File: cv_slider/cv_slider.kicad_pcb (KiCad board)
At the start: 2 copper layers, 47 x 8.2 mm, 12 parts, among them J1 I/O connector, U1 HT7550-1, U2 TLV6001UIDBVR

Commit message: Added 1k output resistor
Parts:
- added R2: 10K, Resistor_SMD:R_0402_1005Metric, F.Cu at (155.4, 81.6)
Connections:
- U2 pad 3: OUT -> Net-(U2-Pad3)
- U2 pad 4: OUT -> Net-(U2-Pad3)
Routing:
- net Net-(U2-Pad3): track 0.00 -> 20.1 mm, vias 0 -> 2
- net OUT: track 21.2 -> 3.26 mm, vias 2 -> 0
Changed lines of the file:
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@@
   (net 6 "OUT")
   (net 7 "Net-(JP1-Pad2)")
+  (net 8 "Net-(U2-Pad3)")
+  (footprint "Resistor_SMD:R_0402_1005Metric" (layer "F.Cu")
+    (at 155.4 81.6 -90)
+    (descr "Resistor SMD 0402 (1005 Metric), square (rectangular) end terminal, IPC_7351 nominal, (Body size source: IPC-SM-782 page 72, https://www.pcb-3d.com/wordpress/wp-content/uploads/ipc-sm-782a_amendment_1_and_2.pdf), generated with kicad-footprint-generator")
+    (tags "resistor")
+    (property "LCSC" "C11702")
+    (property "Sheetfile" "File: cv_slider.kicad_sch")
+    (property "Sheetname" "")
+    (attr smd)
+    (fp_text reference "R2" (at 0 -1.17 90) (layer "F.SilkS") hide
+      (effects (font (size 1 1) (thickness 0.15)))
+    )
+    (fp_text value "10K" (at 0 1.17 90) (layer "F.Fab")
+      (effects (font (size 1 1) (thickness 0.15)))
+    )
+    (fp_text user "${REFERENCE}" (at 0 0 90) (layer "F.Fab")
+      (effects (font (size 0.26 0.26) (thickness 0.04)))
+    )
+    (fp_line (start -0.153641 -0.38) (end 0.153641 -0.38) (layer "F.SilkS") (width 0.12))
+    (fp_line (start -0.153641 0.38) (end 0.153641 0.38) (layer "F.SilkS") (width 0.12))
+    (fp_line (start -0.93 0.47) (end -0.93 -0.47) (layer "F.CrtYd") (width 0.05))
+    (fp_line (start -0.93 -0.47) (end 0.93 -0.47) (layer "F.CrtYd") (width 0.05))
+    (fp_line (start 0.93 -0.47) (end 0.93 0.47) (layer "F.CrtYd") (width 0.05))
+    (fp_line (start 0.93 0.47) (end -0.93 0.47) (layer "F.CrtYd") (width 0.05))
+    (fp_line (start -0.525 0.27) (end -0.525 -0.27) (layer "F.Fab") (width 0.1))
+    (fp_line (start -0.525 -0.27) (end 0.525 -0.27) (layer "F.Fab") (width 0.1))
+    (fp_line (start 0.525 0.27) (end -0.525 0.27) (layer "F.Fab") (width 0.1))
+    (fp_line (start 0.525 -0.27) (end 0.525 0.27) (layer "F.Fab") (width 0.1))
+    (pad "1" smd roundrect (at -0.51 0 270) (size 0.54 0.64) (layers "F.Cu" "F.Paste" "F.Mask") (roundrect_rratio 0.25)
+      (net 8 "Net-(U2-Pad3)") (pintype "passive"))
+    (pad "2" smd roundrect (at 0.51 0 270) (size 0.54 0.64) (layers "F.Cu" "F.Paste" "F.Mask") (roundrect_rratio 0.25)
+      (net 6 "OUT") (pintype "passive"))
+    (model "${KICAD6_3DMODEL_DIR}/Resistor_SMD.3dshapes/R_0402_1005Metric.wrl"
+      (offset (xyz 0 0 0))
+      (scale (xyz 1 1 1))
+      (rotate (xyz 0 0 0))
+    )
+  )
   (footprint "cycfi_library:pin_header_1x3p_2.54mm_smd_horizontal" (layer "F.Cu")
     (at 152.8 83.7 180)
@@
     (descr "SOT, 5 Pin (https://www.jedec.org/sites/default/files/docs/Mo-178c.PDF variant AA), generated with kicad-footprint-generator ipc_gullwing_generator.py")
     (tags "SOT TO_SOT_SMD")
+    (property "LCSC" "C544299")
     (property "Sheetfile" "File: cv_slider.kicad_sch")
     (property "Sheetname" "")
@@
       (net 2 "GND") (pinfunction "V-") (pintype "power_in"))
     (pad "3" smd roundrect (at -1.1375 0.95 270) (size 1.325 0.6) (layers "F.Cu" "F.Paste" "F.Mask") (roundrect_rratio 0.25)
-      (net 6 "OUT") (pinfunction "-") (pintype "input"))
+      (net 8 "Net-(U2-Pad3)") (pinfunction "-") (pintype "input"))
     (pad "4" smd roundrect (at 1.1375 0.95 270) (size 1.325 0.6) (layers "F.Cu" "F.Paste" "F.Mask") (roundrect_rratio 0.25)
-      (net 6 "OUT") (pintype "output"))
+      (net 8 "Net-(U2-Pad3)") (pintype "output"))
     (pad "5" smd roundrect (at 1.1375 -0.95 270) (size 1.325 0.6) (layers "F.Cu" "F.Paste" "F.Mask") (roundrect_rratio 0.25)
       (net 3 "5v") (pinfunction "V+") (pintype "power_in"))
@@
     )
   )
-  (footprint "cycfi_library:cycfi-logo-9mm" locked (layer "F.Cu")
+  (footprint "cycfi_library:cycfi-logo-9mm" (layer "F.Cu")
     (at 141.5 83)
-    (attr through_hole)
+    (attr through_hole board_only)
     (fp_text reference "G***" (at 0 0) (layer "F.SilkS") hide
       (effects (font (size 1.524 1.524) (thickness 0.3)))
@@
   (segment (start 152.8 78.62) (end 155.63 78.62) (width 0.4084) (layer "F.Cu") (net 5))
   (segment (start 155.63 78.62) (end 155.65 78.6) (width 0.4084) (layer "F.Cu") (net 5))
-  (segment (start 169.5125 82.3375) (end 168.85 83) (width 0.4084) (layer "F.Cu") (net 6))
-  (segment (start 155.25 82.35) (end 154.15 82.35) (width 0.4084) (layer "F.Cu") (net 6))
-  (segment (start 154.15 82.35) (end 152.8 83.7) (width 0.4084) (layer "F.Cu") (net 6))
-  (segment (start 170.05 82.3375) (end 170.05 80.0625) (width 0.4084) (layer "F.Cu") (net 6))
-  (segment (start 170.05 82.3375) (end 169.5125 82.3375) (width 0.4084) (layer "F.Cu") (net 6))
-  (via (at 168.85 83) (size 0.6) (drill 0.4) (layers "F.Cu" "B.Cu") (net 6))
-  (via (at 155.25 82.35) (size 0.6) (drill 0.4) (layers "F.Cu" "B.Cu") (net 6))
-  (segment (start 155.9542 81.6458) (end 155.25 82.35) (width 0.4084) (layer "B.Cu") (net 6))
-  (segment (start 167.4958 81.6458) (end 155.9542 81.6458) (width 0.4084) (layer "B.Cu") (net 6))
-  (segment (start 168.85 83) (end 167.4958 81.6458) (width 0.4084) (layer "B.Cu") (net 6))
+  (segment (start 154.39 82.11) (end 155.4 82.11) (width 0.4084) (layer "F.Cu") (net 6))
+  (segment (start 152.8 83.7) (end 154.39 82.11) (width 0.4084) (layer "F.Cu") (net 6))
   (segment (start 168 81.56) (end 168 83.7) (width 0.4084) (layer "F.Cu") (net 7))
   (segment (start 167.1 84.6) (end 164.575 84.6) (width 0.4084) (layer "F.Cu") (net 7))
   (segment (start 168 83.7) (end 167.1 84.6) (width 0.4084) (layer "F.Cu") (net 7))
   (segment (start 164.575 84.6) (end 163.875 83.9) (width 0.4084) (layer "F.Cu") (net 7))
+  (segment (start 155.3 80.1) (end 155.3 80.99) (width 0.4084) (layer "F.Cu") (net 8))
+  (segment (start 155.3 80.99) (end 155.4 81.09) (width 0.4084) (layer "F.Cu") (net 8))
+  (segment (start 169.5125 82.3375) (end 168.85 83) (width 0.4084) (layer "F.Cu") (net 8))
+  (segment (start 170.05 82.3375) (end 170.05 80.0625) (width 0.4084) (layer "F.Cu") (net 8))
+  (segment (start 170.05 82.3375) (end 169.5125 82.3375) (width 0.4084) (layer "F.Cu") (net 8))
+  (via (at 168.85 83) (size 0.6) (drill 0.4) (layers "F.Cu" "B.Cu") (net 8))
+  (via (at 155.3 80.1) (size 0.6) (drill 0.4) (layers "F.Cu" "B.Cu") (net 8))
+  (segment (start 155.9542 81.6458) (end 155.9542 80.7542) (width 0.4084) (layer "B.Cu") (net 8))
+  (segment (start 167.4958 81.6458) (end 155.9542 81.6458) (width 0.4084) (layer "B.Cu") (net 8))
+  (segment (start 168.85 83) (end 167.4958 81.6458) (width 0.4084) (layer "B.Cu") (net 8))
+  (segment (start 155.9542 80.7542) (end 155.3 80.1) (width 0.4084) (layer "B.Cu") (net 8))
   (zone (net 2) (net_name "GND") (layers F&B.Cu) (hatch edge 0.508)
     (connect_pads (clearance 0.3))

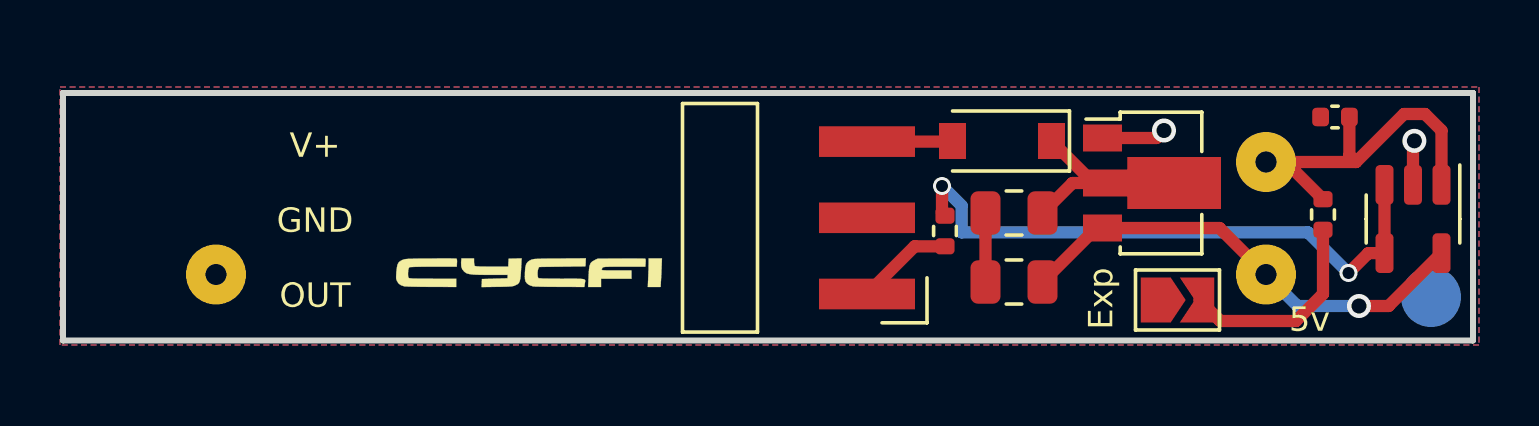
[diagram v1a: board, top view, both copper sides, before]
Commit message: Fabricating cv-slider prototype
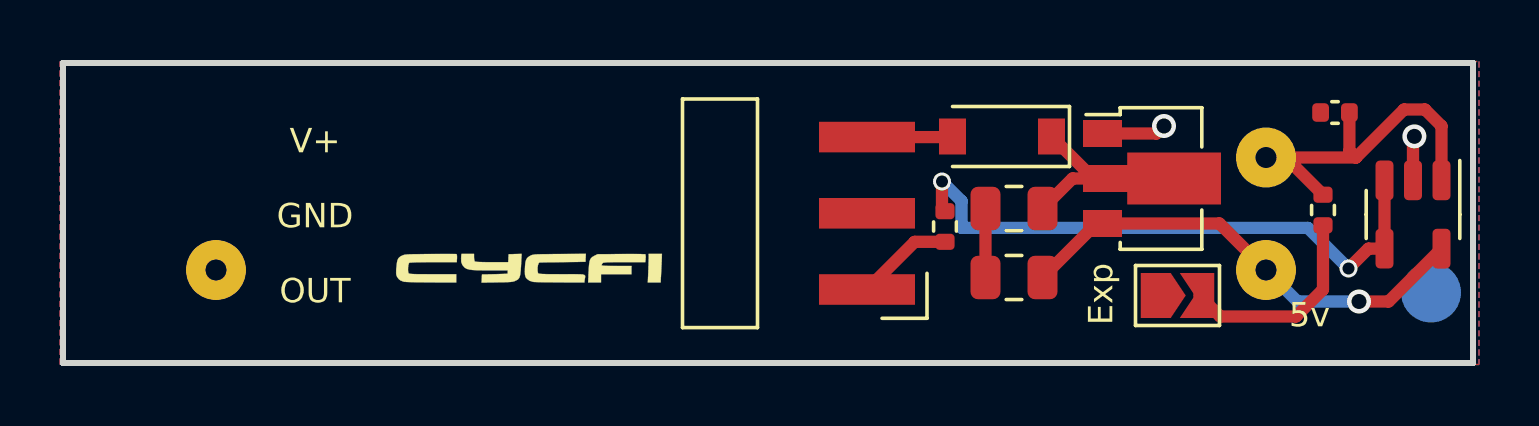
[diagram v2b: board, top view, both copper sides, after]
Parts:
- R2: value 10K -> 1K
- moved J1 2.69 mm to (152.8, 81.0)
- moved C1 0.15 mm to (157.7, 80.8)
- moved G*** 0.15 mm to (141.5, 82.8)
- moved JP1 0.15 mm to (163.2, 83.8)
- moved U1 0.15 mm to (162.3, 79.8)
- moved U2 0.15 mm to (171.0, 81.0)
- moved C2 0.15 mm to (157.7, 83.2)
- moved C3 0.15 mm to (168.4, 77.7)
- moved D1 0.15 mm to (157.3, 78.5)
- moved H1 0.15 mm to (171.6, 83.7)
- moved R1 0.15 mm to (168.0, 80.9)
- moved R2 0.15 mm to (155.4, 81.5)
- moved RV1 0.15 mm to (148.6, 81.0)
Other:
- board size 47 x 8.2 mm -> 47 x 10 mm
- board text removed: "<- Pot Body"

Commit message: PCB manufacturing adjustments
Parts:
- removed H1: Ground Pad, cycfi_library:single-pad-2x2-circular
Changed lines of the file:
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@@
   (footprint "cycfi_library:pin_header_1x3p_2.54mm_smd_horizontal" (layer "F.Cu")
     (at 152.8 81.01 180)
+    (property "JLCPCB_CORRECTION" "0;0;90")
+    (property "LCSC" "C5242196")
     (property "Sheetfile" "File: cv_slider.kicad_sch")
     (property "Sheetname" "")
@@
     (descr "SOT, 5 Pin (https://www.jedec.org/sites/default/files/docs/Mo-178c.PDF variant AA), generated with kicad-footprint-generator ipc_gullwing_generator.py")
     (tags "SOT TO_SOT_SMD")
+    (property "JLCPCB_CORRECTION" "0;0;180")
     (property "LCSC" "C544299")
     (property "Sheetfile" "File: cv_slider.kicad_sch")
@@
     (descr "SOT-89-3, http://ww1.microchip.com/downloads/en/DeviceDoc/3L_SOT-89_MB_C04-029C.pdf")
     (tags "SOT-89-3")
+    (property "JLCPCB_CORRECTION" "0;0;180")
     (property "LCSC" "C16106")
     (property "Sheetfile" "File: cv_slider.kicad_sch")
@@
     )
     (fp_rect (start -22.5 4) (end 22.5 -4) (layer "B.CrtYd") (width 0.12) (fill none))
-    (pad "1" thru_hole circle (at -17.5 -1.875 180) (size 2 2) (drill 0.7) (layers *.Cu *.Mask)
+    (pad "1" thru_hole circle (at -17.5 -1.875 180) (size 2 2) (drill 1) (layers *.Cu *.Mask)
       (net 3 "5v") (pinfunction "1") (pintype "passive"))
-    (pad "2" thru_hole circle (at -17.5 1.875 180) (size 2 2) (drill 0.7) (layers *.Cu *.Mask)
+    (pad "2" thru_hole circle (at -17.5 1.875 180) (size 2 2) (drill 1) (layers *.Cu *.Mask)
       (net 4 "/pot_center") (pinfunction "2") (pintype "passive"))
-    (pad "3" thru_hole circle (at 17.5 -1.875 180) (size 2 2) (drill 0.7) (layers *.Cu *.Mask)
+    (pad "3" thru_hole circle (at 17.5 -1.875 180) (size 2 2) (drill 1) (layers *.Cu *.Mask)
       (net 2 "GND") (pinfunction "3") (pintype "passive"))
-  )
-  (footprint "cycfi_library:single-pad-2x2-circular" (layer "B.Cu")
-    (at 171.6 83.65 180)
-    (property "Sheetfile" "File: cv_slider.kicad_sch")
-    (property "Sheetname" "")
-    (attr through_hole)
-    (fp_text reference "H1" (at 0 -2.54) (layer "B.SilkS") hide
-      (effects (font (size 1 1) (thickness 0.15)) (justify mirror))
-    )
-    (fp_text value "Ground Pad" (at 0 2.54) (layer "B.Fab") hide
-      (effects (font (size 1 1) (thickness 0.15)) (justify mirror))
-    )
-    (pad "1" smd circle (at 0 0 180) (size 2 2) (layers "B.Cu" "B.Paste" "B.Mask")
-      (net 2 "GND") (pinfunction "1") (pintype "input"))
   )
   (gr_rect (start 126 76) (end 173 86) (layer "Edge.Cuts") (width 0.2) (fill none))
@@
   (via (at 168.85 82.85) (size 0.6) (drill 0.4) (layers "F.Cu" "B.Cu") (net 8))
   (via (at 155.3 79.95) (size 0.6) (drill 0.4) (layers "F.Cu" "B.Cu") (net 8))
-  (segment (start 155.9542 81.4958) (end 155.9542 80.6042) (width 0.4084) (layer "B.Cu") (net 8))
-  (segment (start 167.4958 81.4958) (end 155.9542 81.4958) (width 0.4084) (layer "B.Cu") (net 8))
+  (segment (start 156.3358 81.4958) (end 155.3 80.46) (width 0.4084) (layer "B.Cu") (net 8))
   (segment (start 168.85 82.85) (end 167.4958 81.4958) (width 0.4084) (layer "B.Cu") (net 8))
-  (segment (start 155.9542 80.6042) (end 155.3 79.95) (width 0.4084) (layer "B.Cu") (net 8))
+  (segment (start 167.4958 81.4958) (end 156.3358 81.4958) (width 0.4084) (layer "B.Cu") (net 8))
+  (segment (start 155.3 80.46) (end 155.3 79.95) (width 0.4084) (layer "B.Cu") (net 8))
   (zone (net 2) (net_name "GND") (layers F&B.Cu) (hatch edge 0.508)
     (connect_pads (clearance 0.3))

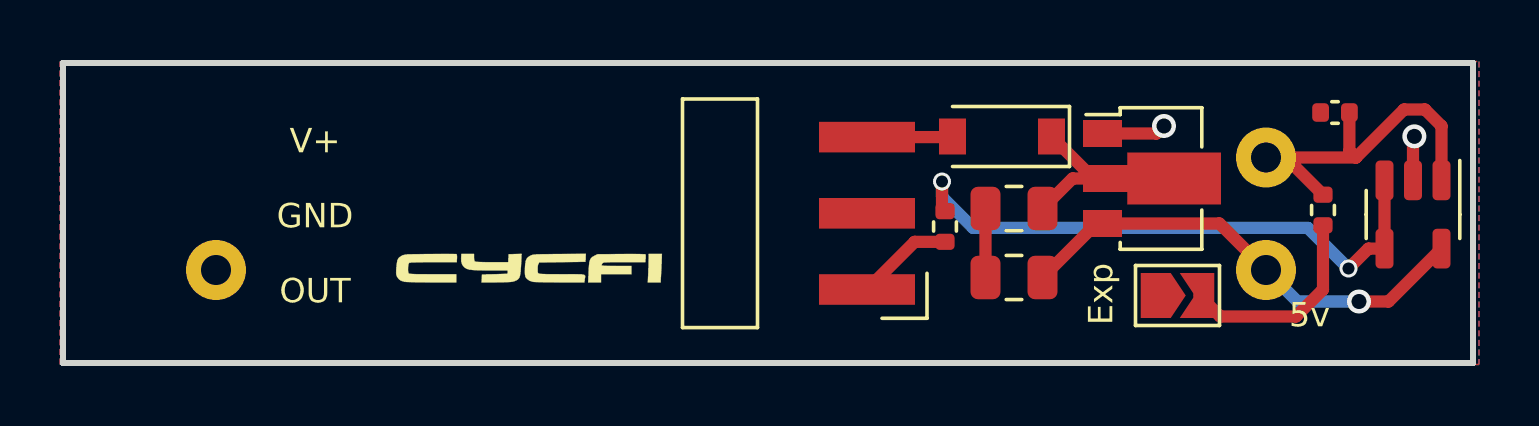
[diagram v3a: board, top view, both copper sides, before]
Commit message: Update v1.1 - Added EXP and LOG taper shunts
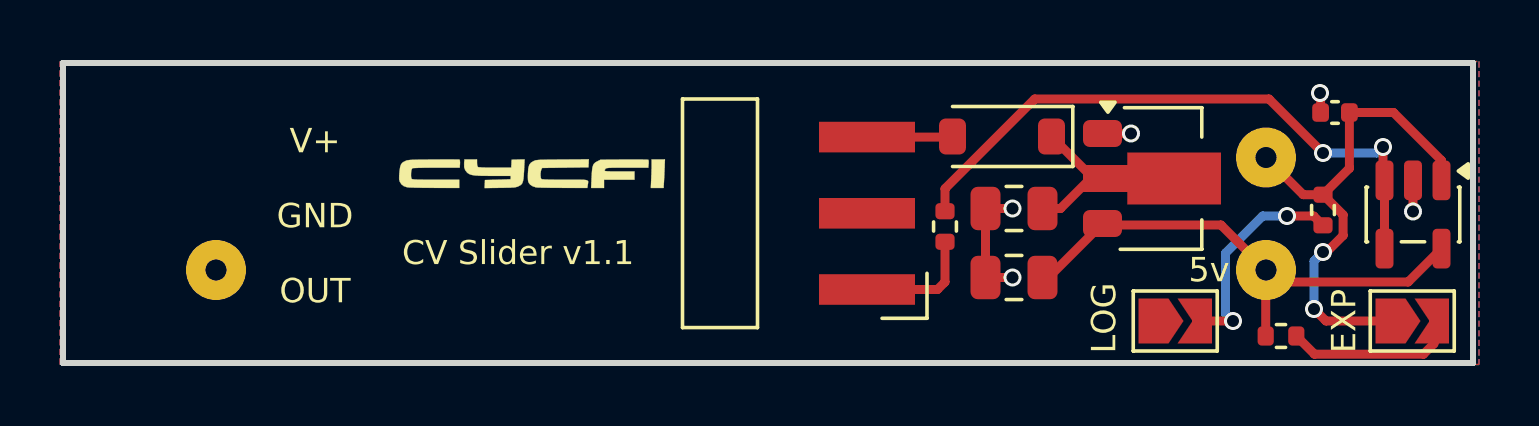
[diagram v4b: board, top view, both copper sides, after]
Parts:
- added JP2: exp shunt, Jumper:SolderJumper-2_P1.3mm_Open_TrianglePad1.0x1.5mm, F.Cu at (171.0, 84.6)
- added R3: 2k, Resistor_SMD:R_0402_1005Metric, F.Cu at (166.6, 85.1)
- JP1: value exp shunt -> log shunt
- moved G*** 3.15 mm to (141.6, 79.7)
- moved JP1 0.85 mm to (163.1, 84.6)
- moved U1 0.30 mm to (162.6, 79.8)
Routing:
- net Net-(JP2-B): track 0.00 -> 5.74 mm
- net /pot_center: track 12.6 -> 17.2 mm, vias 0 -> 2
- net 5v: track 15.9 -> 17.5 mm, vias 1 -> 0
- net Net-(U2--): track 19.8 -> 20.8 mm
- net GND: track 5.94 -> 6.75 mm, vias 2 -> 5
- net OUT: track 3.26 -> 4.04 mm
- net Net-(JP1-B): track 6.93 -> 7.46 mm, vias 0 -> 2
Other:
- rule pad_to_mask_clearance: 0.2 -> 0
- board text added: "CV Slider v1.1"
- board text added: "EXP"
- board text added: "LOG"
- board text removed: "Exp"
